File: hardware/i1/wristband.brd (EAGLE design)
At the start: 51.9 x 27.6 mm, 9 parts, among them M1 MOTOR10MM, Q1 600mA/40V

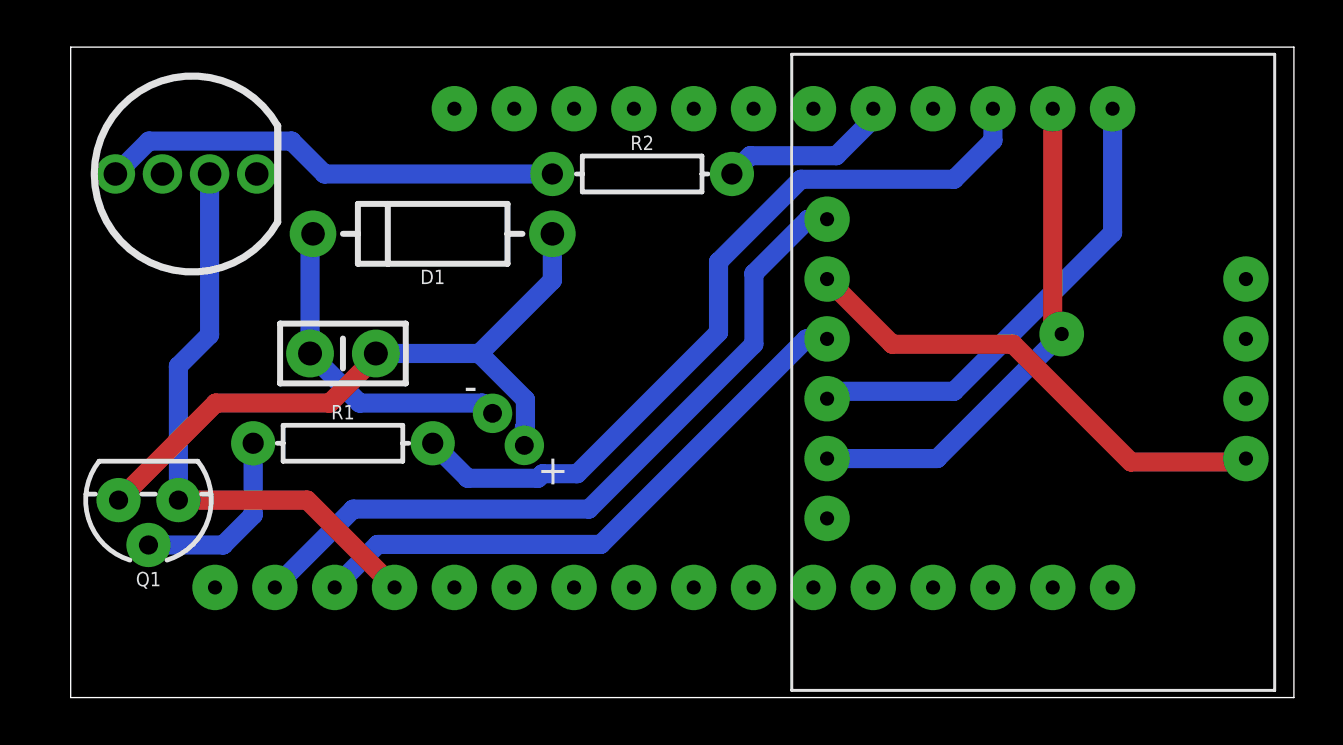
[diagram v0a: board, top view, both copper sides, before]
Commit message: Tighten components to allow for mounting holes
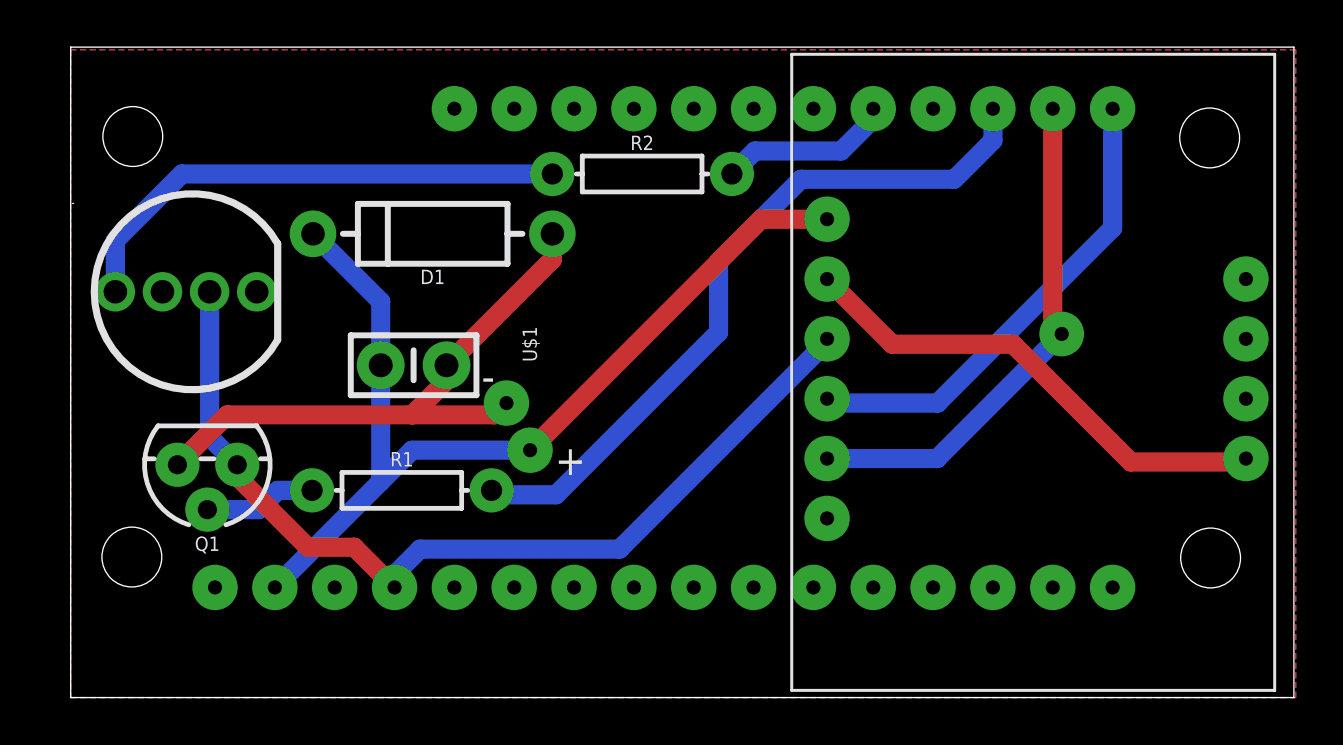
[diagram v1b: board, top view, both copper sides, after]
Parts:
- removed M1: MOTOR10MM, SparkFun-Electromechanical:VIBE-MOTOR-10MM
- added U$1: VIBRATION_MOTOR, my_library:VIBRATION_MOTOR
- moved RGB_LED1 5.00 mm to (1.40, 17.2)
- moved R1 3.20 mm to (14.1, 8.79)
- moved C1 3.04 mm to (14.6, 14.1)
- moved Q1 2.92 mm to (5.80, 9.88)
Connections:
- removed net N$12: C1.1, D1.C, M1.-
- removed net N$4: BF1.ARF, BNO1.GND
- removed net N$6: BF1.GND, Q1.1, RGB_LED1.GND
- new net GND: BF1.GND, BNO1.GND, Q1.1, RGB_LED1.GND
- net N$3: now also C1.1, D1.C, U$1.+
- net N$9: now also U$1.-; no longer M1.+
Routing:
- net GND: track 0.00 -> 40.1 mm
- net N$4: track 25.3 -> 0.00 mm
- net N$6: track 25.1 -> 0.00 mm
- net N$12: track 13.9 -> 0.00 mm
- net N$3: track 31.7 -> 41.6 mm
- net N$9: track 29.1 -> 25.2 mm
- net N$10: track 8.02 -> 4.78 mm
- net N$11: track 33.4 -> 30.7 mm
- net N$7: track 19.7 -> 21.9 mm
- added copper zone on layer 1, net GND
- added copper zone on layer 16, net GND

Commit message: Final tweaks for mechanical fit.
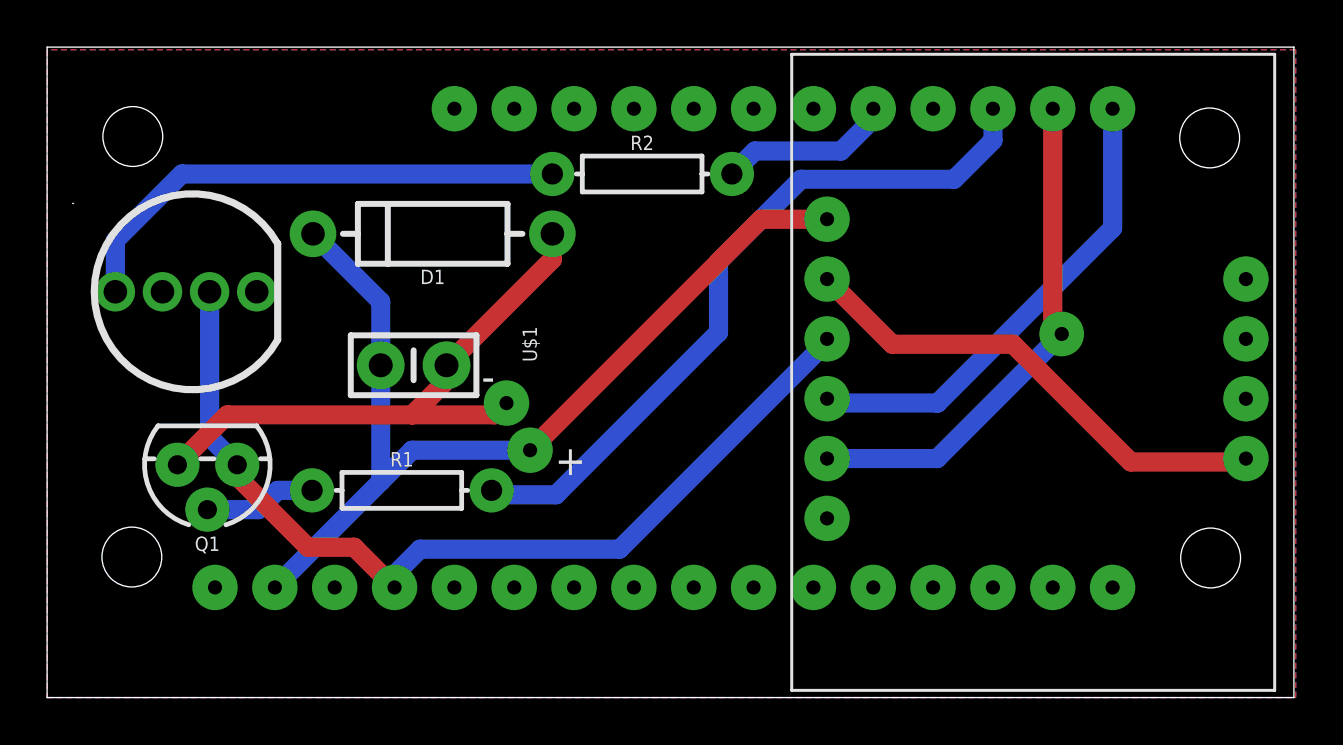
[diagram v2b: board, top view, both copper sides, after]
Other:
- board size 51.9 x 27.6 mm -> 52.9 x 27.6 mm
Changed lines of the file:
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@@
 <board>
 <plain>
-<wire x1="0" y1="0" x2="51.923" y2="0" width="0" layer="20"/>
+<wire x1="-1" y1="0" x2="51.923" y2="0" width="0" layer="20"/>
 <wire x1="51.923" y1="0" x2="51.923" y2="27.61" width="0" layer="20"/>
-<wire x1="51.923" y1="27.61" x2="0" y2="27.61" width="0" layer="20"/>
-<wire x1="0" y1="27.61" x2="0" y2="0" width="0" layer="20"/>
+<wire x1="51.923" y1="27.61" x2="-1" y2="27.61" width="0" layer="20"/>
+<wire x1="-1" y1="27.61" x2="-1" y2="0" width="0" layer="20"/>
 </plain>
 <attributes>
@@
 <wire x1="12.04" y1="6.382" x2="13.747" y2="4.675" width="0.8128" layer="1"/>
 <polygon width="0.0762" layer="1">
-<vertex x="0" y="27.5"/>
-<vertex x="0" y="0"/>
+<vertex x="-1" y="27.5"/>
+<vertex x="-1" y="0"/>
 <vertex x="52" y="0"/>
 <vertex x="52" y="27.5"/>
 </polygon>
 <polygon width="0.0762" layer="16">
-<vertex x="0" y="27.5"/>
-<vertex x="0" y="0"/>
+<vertex x="-1" y="27.5"/>
+<vertex x="-1" y="0"/>
 <vertex x="52" y="0"/>
 <vertex x="52" y="27.5"/>
